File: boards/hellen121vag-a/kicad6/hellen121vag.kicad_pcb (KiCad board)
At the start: 2 copper layers, 164 x 118 mm, 9 parts, among them M1 Module-can-0.1, M2 Module-power5-0.1, M3 Module-mcu-0.1, M4 Module-input-0.1, M5 Module-knock-0.1, M6 Module-output-0.1, M7 Module-ign8-0.1, M8 Module-power12-0.1, P1 368255-2

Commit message: fresh kicad files
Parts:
- added C1: Cap, hellen-one-common:C0603, F.Cu at (115.7, 11.3)
- added D1: D_TVS_Array_4, hellen-one-common:SOT23-6, F.Cu at (121.5, 64.8)
- added F1: Fuse-Pad-Pad, hellen-one-common:PAD-1206-PAD, F.Cu at (188.1, 81.3)
- added F2: Fuse-Pad-Pad, hellen-one-common:PAD-1206-PAD, F.Cu at (183.9, 81.4)
- added J1: USB_B_Mini, hellen-one-common:USB-MINI-B-VERTICAL, F.Cu at (127.3, 9.27)
- added R1: Res_Array_4, hellen-one-common:R0603-4, F.Cu at (124.9, 64.7)
- added R2: Jumper-Pad-Pad, hellen-one-common:PAD-0805-PAD, F.Cu at (90.6, 82.1)
- added R3: Jumper-Pad-Pad, hellen-one-common:PAD-0805-PAD, F.Cu at (87.5, 82.4)
- added R4: Jumper-Pad-Pad, hellen-one-common:PAD-0805-PAD, F.Cu at (100.3, 82.2)
- added R5: Res_Array_4, hellen-one-common:R0603-4, F.Cu at (118.3, 64.7)
- added R6: Res, hellen-one-common:R0603, F.Cu at (102.6, 69.4)
- added R7: Res, hellen-one-common:R0603, F.Cu at (101.2, 69.4)
- added R8: Jumper-Pad-Pad, hellen-one-common:PAD-0805-PAD, F.Cu at (95.2, 82.3)
- added R9: Jumper-Pad-Pad, hellen-one-common:PAD-0805-PAD, F.Cu at (75.9, 82.6)
- added S1: Button_SPST, hellen-one-common:SMD-2_2.9x3.9x1.7, F.Cu at (112.1, 6.44)
- added S2: Button_SPST, hellen-one-common:SMD-2_2.9x3.9x1.7, F.Cu at (116.0, 6.42)
- added V10: Pad, hellen-one-common:PAD-TH, F.Cu at (122.6, 77.9)
- added V11: Pad, hellen-one-common:PAD-TH, F.Cu at (117.5, 77.9)
- added V12: Pad, hellen-one-common:PAD-TH, F.Cu at (113.0, 82.1)
- added V13: Pad, hellen-one-common:PAD-TH, F.Cu at (108.0, 82.1)
- added V14: Pad, hellen-one-common:PAD-TH, F.Cu at (104.9, 77.8)
- added V17: Pad, hellen-one-common:PAD-TH, F.Cu at (102.9, 82.1)
- added V20: Pad, hellen-one-common:PAD-TH, F.Cu at (95.5, 77.7)
- added V28: Pad, hellen-one-common:PAD-TH, F.Cu at (125.1, 77.9)
- added V40: Pad, hellen-one-common:PAD-TH, F.Cu at (93.0, 77.7)
- added V41: Pad, hellen-one-common:PAD-TH, F.Cu at (90.5, 77.7)
- added V43: Pad, hellen-one-common:PAD-TH, F.Cu at (85.5, 77.7)
- added V44: Pad, hellen-one-common:PAD-TH, F.Cu at (131.4, 77.9)
- added V45: Pad, hellen-one-common:PAD-TH, F.Cu at (129.3, 82.5)
- added V46: Pad, hellen-one-common:PAD-TH, F.Cu at (126.1, 82.5)
- added V48: Pad, hellen-one-common:PAD-TH, F.Cu at (120.0, 77.9)
- added V49: Pad, hellen-one-common:PAD-TH, F.Cu at (119.3, 82.4)
- added V51: Pad, hellen-one-common:PAD-TH, F.Cu at (110.5, 82.1)
- added V52: Pad, hellen-one-common:PAD-TH, F.Cu at (105.4, 82.1)
- added V56: Pad, hellen-one-common:PAD-TH, F.Cu at (101.7, 77.8)
- added V61: Pad, hellen-one-common:PAD-TH, F.Cu at (88.0, 77.7)
- added V63: Pad, hellen-one-common:PAD-TH, F.Cu at (133.4, 82.4)
- added V64: Pad, hellen-one-common:PAD-TH, F.Cu at (127.7, 77.9)
- added V66: Pad, hellen-one-common:PAD-TH, F.Cu at (139.2, 73.8)
- added V67: Pad, hellen-one-common:PAD-TH, F.Cu at (134.5, 77.8)
- added V68: Pad, hellen-one-common:PAD-TH, F.Cu at (137.7, 77.7)
- added V69: Pad, hellen-one-common:PAD-TH, F.Cu at (137.7, 82.1)
- added V70: Pad, hellen-one-common:PAD-TH, F.Cu at (140.8, 77.7)
- added V71: Pad, hellen-one-common:PAD-TH, F.Cu at (140.9, 82.1)
- added V74: Pad, hellen-one-common:PAD-TH, F.Cu at (80.4, 77.8)
- added V80: Pad, hellen-one-common:PAD-TH, F.Cu at (82.9, 77.7)
- added V9: Pad, hellen-one-common:PAD-TH, F.Cu at (122.9, 82.4)
- added VIN1: Pad, hellen-one-common:PAD-TH, F.Cu at (90.7, 68.8)
- added VIN2: Pad, hellen-one-common:PAD-TH, F.Cu at (99.2, 68.8)
- added VIN3: Pad, hellen-one-common:PAD-TH, F.Cu at (96.4, 68.8)
- added VIN4: Pad, hellen-one-common:PAD-TH, F.Cu at (93.5, 68.8)
- added VOUT1: Pad, hellen-one-common:PAD-TH, F.Cu at (152.9, 76.0)
- added VOUT2: Pad, hellen-one-common:PAD-TH, F.Cu at (162.4, 75.6)
- added VOUT3: Pad, hellen-one-common:PAD-TH, F.Cu at (166.0, 75.8)
- moved M5 23.3 mm to (64.3, 54.8)
- moved M8 12.0 mm to (120.8, 67.7)
- moved M6 10.8 mm to (140.8, 66.4)
- moved M7 9.92 mm to (72.4, 26.8)
- moved M4 9.40 mm to (85.0, 66.7)
- moved M3 8.56 mm to (84.9, 51.4)
- moved M1 1.99 mm to (85.2, 13.1)
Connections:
- M1 pad S1: unconnected-(M1-PadS1) -> /CANL
- M1 pad S2: unconnected-(M1-PadS2) -> /CANH
- M3 pad E10: unconnected-(M3-PadE10) -> /VVT1_1
- M3 pad E12: unconnected-(M3-PadE12) -> /WASTEGATE
- M3 pad E14: unconnected-(M3-PadE14) -> /COIL_A1
- M3 pad E15: unconnected-(M3-PadE15) -> /COIL_A2
- M3 pad E16: unconnected-(M3-PadE16) -> /VVT2_B1
- M3 pad E17: unconnected-(M3-PadE17) -> /VVT2_B2
- M3 pad E18: unconnected-(M3-PadE18) -> /IDLE
- M3 pad E19: unconnected-(M3-PadE19) -> /FUEL_CONSUM
- M3 pad E20: unconnected-(M3-PadE20) -> /VVT1_1
- M3 pad E21: unconnected-(M3-PadE21) -> /VVT1_2
- M3 pad E22: unconnected-(M3-PadE22) -> /CE
- M3 pad E25: unconnected-(M3-PadE25) -> /INJ1
- M3 pad E26: unconnected-(M3-PadE26) -> /INJ2
- M3 pad E27: unconnected-(M3-PadE27) -> /TACH
- M3 pad E28: unconnected-(M3-PadE28) -> /OUT3
- M3 pad E29: unconnected-(M3-PadE29) -> /INJ3
- M3 pad E30: unconnected-(M3-PadE30) -> /INJ4
- M3 pad E31: unconnected-(M3-PadE31) -> /INJ5
- M3 pad E32: unconnected-(M3-PadE32) -> /INJ6
- M3 pad E33: unconnected-(M3-PadE33) -> /INJ7
- M3 pad E34: unconnected-(M3-PadE34) -> /INJ8
- M3 pad E6: unconnected-(M3-PadE6) -> /MAIN
- M3 pad E7: unconnected-(M3-PadE7) -> /OUT1
- M3 pad E8: unconnected-(M3-PadE8) -> /PUMP
- M3 pad E9: unconnected-(M3-PadE9) -> /OUT2
- M3 pad N14: unconnected-(M3-PadN14) -> +3V3
- M3 pad N22: unconnected-(M3-PadN22) -> /NRESET
- M3 pad N26: unconnected-(M3-PadN26) -> /BOOT0
- M3 pad N27: unconnected-(M3-PadN27) -> /VBUS
- M3 pad N28: unconnected-(M3-PadN28) -> /USBP
- M3 pad N29: unconnected-(M3-PadN29) -> /USBM
- M3 pad S12: unconnected-(M3-PadS12) -> /KNOCK1
- M3 pad S13: unconnected-(M3-PadS13) -> /CRANK
- M3 pad S14: unconnected-(M3-PadS14) -> /VSS
- M3 pad S15: unconnected-(M3-PadS15) -> /CAM1
- M3 pad S16: unconnected-(M3-PadS16) -> /O2S
- M3 pad S17: unconnected-(M3-PadS17) -> /TPS1
- M3 pad S18: unconnected-(M3-PadS18) -> /CLT
- M3 pad S19: unconnected-(M3-PadS19) -> /IAT
- M3 pad S20: unconnected-(M3-PadS20) -> /MAF
- M3 pad S21: unconnected-(M3-PadS21) -> /MAP2
- M3 pad S22: unconnected-(M3-PadS22) -> /A2
- M3 pad S23: unconnected-(M3-PadS23) -> /A4
- M3 pad S24: unconnected-(M3-PadS24) -> /TPS2
- M3 pad S25: unconnected-(M3-PadS25) -> /PPS2
- M3 pad S26: unconnected-(M3-PadS26) -> /A3
- M3 pad S27: unconnected-(M3-PadS27) -> /CAM2
- M3 pad S28: unconnected-(M3-PadS28) -> /RES1
- M3 pad S29: unconnected-(M3-PadS29) -> /PPS1
- M3 pad S3: unconnected-(M3-PadS3) -> /D1
- M3 pad S30: unconnected-(M3-PadS30) -> /A1
- M3 pad S31: unconnected-(M3-PadS31) -> /RES2
- M3 pad S33: +5V -> V5A
- M3 pad S4: unconnected-(M3-PadS4) -> /D2
- M3 pad S5: unconnected-(M3-PadS5) -> /D3
- M3 pad S6: unconnected-(M3-PadS6) -> /D4
- M4 pad E6: +5V -> V5A
- M4 pad J1: +5V -> V5A
- M4 pad J10: unconnected-(M4-PadJ10) -> V5A
- M4 pad J11: unconnected-(M4-PadJ11) -> GNDA
- M4 pad J12: unconnected-(M4-PadJ12) -> GNDA
- M4 pad J13: unconnected-(M4-PadJ13) -> GNDA
- M4 pad J14: unconnected-(M4-PadJ14) -> GNDA
- M4 pad J17: unconnected-(M4-PadJ17) -> V5A
- M4 pad J18: unconnected-(M4-PadJ18) -> V5A
- M4 pad J19: unconnected-(M4-PadJ19) -> V5A
- M4 pad J20: unconnected-(M4-PadJ20) -> V5A
- M4 pad J21: unconnected-(M4-PadJ21) -> V5A
- M4 pad J22: unconnected-(M4-PadJ22) -> GNDA
- M4 pad J24: unconnected-(M4-PadJ24) -> GNDA
- M4 pad J3: unconnected-(M4-PadJ3) -> GNDA
- M4 pad J4: unconnected-(M4-PadJ4) -> GNDA
- M4 pad J5: unconnected-(M4-PadJ5) -> V5A
- M4 pad J6: unconnected-(M4-PadJ6) -> GNDA
- M4 pad J7: unconnected-(M4-PadJ7) -> V5A
- M4 pad J8: unconnected-(M4-PadJ8) -> GNDA
- M4 pad J9: unconnected-(M4-PadJ9) -> V5A
- M4 pad N1: unconnected-(M4-PadN1) -> V5A
- M4 pad N10: unconnected-(M4-PadN10) -> /TPS2
- M4 pad N11: unconnected-(M4-PadN11) -> /A4
- M4 pad N12: unconnected-(M4-PadN12) -> /A2
- M4 pad N13: unconnected-(M4-PadN13) -> /MAP2
- M4 pad N14: unconnected-(M4-PadN14) -> /MAF
- M4 pad N15: unconnected-(M4-PadN15) -> /IAT
- M4 pad N16: unconnected-(M4-PadN16) -> /CLT
- M4 pad N17: unconnected-(M4-PadN17) -> /TPS1
- M4 pad N18: unconnected-(M4-PadN18) -> /AFR
- M4 pad N19: unconnected-(M4-PadN19) -> /CAM1
- M4 pad N2: unconnected-(M4-PadN2) -> GNDA
- M4 pad N20: unconnected-(M4-PadN20) -> /VSS
- M4 pad N21: unconnected-(M4-PadN21) -> /CRANK
- M4 pad N22: unconnected-(M4-PadN22) -> /KNOCK1
- M4 pad N24: unconnected-(M4-PadN24) -> /KNOCK2
- M4 pad N3: unconnected-(M4-PadN3) -> /RES2
- M4 pad N4: unconnected-(M4-PadN4) -> /A1
- M4 pad N5: unconnected-(M4-PadN5) -> /PPS1
- M4 pad N6: unconnected-(M4-PadN6) -> /MAF
- M4 pad N7: unconnected-(M4-PadN7) -> /CAM2
- M4 pad N8: unconnected-(M4-PadN8) -> /A3
- M4 pad N9: unconnected-(M4-PadN9) -> /PPS2
- M4 pad S10: unconnected-(M4-PadS10) -> /IN_TPS1
- M4 pad S11: unconnected-(M4-PadS11) -> /IN_MAF
- M4 pad S12: unconnected-(M4-PadS12) -> /IN_MAP2
- M4 pad S13: unconnected-(M4-PadS13) -> /VREF2
- M4 pad S14: unconnected-(M4-PadS14) -> /VREF1
- M4 pad S15: unconnected-(M4-PadS15) -> /IN_CLT
- M4 pad S16: unconnected-(M4-PadS16) -> /IN_IAT
- M4 pad S17: unconnected-(M4-PadS17) -> /IN_TPS2
- M4 pad S18: unconnected-(M4-PadS18) -> /IN_PPS2
- M4 pad S19: unconnected-(M4-PadS19) -> /IN_A2
- M4 pad S20: unconnected-(M4-PadS20) -> /IN_A3
- M4 pad S21: unconnected-(M4-PadS21) -> /IN_CAM2
- M4 pad S22: unconnected-(M4-PadS22) -> /IN_A4
- M4 pad S23: unconnected-(M4-PadS23) -> /IN_RES1
- M4 pad S24: unconnected-(M4-PadS24) -> /IN_PPS1
- M4 pad S25: unconnected-(M4-PadS25) -> /IN_A1
- M4 pad S26: unconnected-(M4-PadS26) -> /IN_RES2
- M4 pad S3: unconnected-(M4-PadS3) -> /IN_KNOCK2
- M4 pad S5: unconnected-(M4-PadS5) -> /IN_CAM1
- M4 pad S6: unconnected-(M4-PadS6) -> /IN_VSS
- M4 pad S7: unconnected-(M4-PadS7) -> /IN_KNOCK1
- M4 pad S8: unconnected-(M4-PadS8) -> /IN_CRANK
- M4 pad S9: unconnected-(M4-PadS9) -> /IN_AFR
- M5 pad E1: +5V -> V5A
- M5 pad E3: unconnected-(M5-PadE3) -> /IN_KNOCK1
- M5 pad W1: unconnected-(M5-PadW1) -> /IN_KNOCK1_RAW
- M5 pad W2: unconnected-(M5-PadW2) -> /VREF2
- M6 pad S1: unconnected-(M6-PadS1) -> /OUT_COIL_A1
- M6 pad S10: unconnected-(M6-PadS10) -> /OUT_PUMP
- M6 pad S11: +5V -> V12_RAW
- M6 pad S12: unconnected-(M6-PadS12) -> Net-(M6-PadS12)
- M6 pad S13: unconnected-(M6-PadS13) -> /OUT_VVT1_1
- M6 pad S14: unconnected-(M6-PadS14) -> /OUT_VVT1_1
- M6 pad S15: unconnected-(M6-PadS15) -> /OUT_INJ6
- M6 pad S16: unconnected-(M6-PadS16) -> /OUT_INJ2
- M6 pad S17: unconnected-(M6-PadS17) -> /OUT_INJ3
- M6 pad S18: unconnected-(M6-PadS18) -> /OUT_INJ1
- M6 pad S2: unconnected-(M6-PadS2) -> /OUT_COIL_A2
- M6 pad S4: unconnected-(M6-PadS4) -> /OUT_VVT2_B1
- M6 pad S5: unconnected-(M6-PadS5) -> /OUT_VVT2_B2
- M6 pad S6: unconnected-(M6-PadS6) -> /OUT_FUEL_CONSUM
- M6 pad S7: unconnected-(M6-PadS7) -> /OUT_IDLE
- M6 pad S8: unconnected-(M6-PadS8) -> Net-(M6-PadS8)
- M6 pad W1: unconnected-(M6-PadW1) -> /OUT_VVT1_2
- M6 pad W10: unconnected-(M6-PadW10) -> /OUT_INJ5
- M6 pad W11: unconnected-(M6-PadW11) -> /OUT_INJ8
- M6 pad W12: unconnected-(M6-PadW12) -> /OUT_INJ7
- M6 pad W13: unconnected-(M6-PadW13) -> /OUT_MAIN
- M6 pad W15: unconnected-(M6-PadW15) -> /INJ8
- M6 pad W16: unconnected-(M6-PadW16) -> /INJ7
- M6 pad W17: unconnected-(M6-PadW17) -> /INJ6
- M6 pad W18: unconnected-(M6-PadW18) -> /INJ5
- M6 pad W19: unconnected-(M6-PadW19) -> /INJ4
- M6 pad W2: unconnected-(M6-PadW2) -> /OUT_VVT1_2
- M6 pad W20: unconnected-(M6-PadW20) -> /INJ3
- M6 pad W21: unconnected-(M6-PadW21) -> /OUT3
- M6 pad W22: unconnected-(M6-PadW22) -> /FUEL_CONSUM
- M6 pad W23: unconnected-(M6-PadW23) -> /INJ2
- M6 pad W24: unconnected-(M6-PadW24) -> /INJ1
- M6 pad W25: unconnected-(M6-PadW25) -> /CE
- M6 pad W26: unconnected-(M6-PadW26) -> /VVT1_2
- M6 pad W27: unconnected-(M6-PadW27) -> /VVT1_1
- M6 pad W28: unconnected-(M6-PadW28) -> /TACH
- M6 pad W29: unconnected-(M6-PadW29) -> /VVT1_2
- M6 pad W3: unconnected-(M6-PadW3) -> /OUT_CE
- M6 pad W30: unconnected-(M6-PadW30) -> /VVT2_B2
- M6 pad W31: unconnected-(M6-PadW31) -> /VVT2_B1
- M6 pad W32: unconnected-(M6-PadW32) -> /COIL_A2
- M6 pad W33: unconnected-(M6-PadW33) -> /COIL_A1
- M6 pad W34: unconnected-(M6-PadW34) -> /WASTEGATE
- M6 pad W35: unconnected-(M6-PadW35) -> /PUMP
- M6 pad W36: unconnected-(M6-PadW36) -> /VVT1_1
- M6 pad W37: unconnected-(M6-PadW37) -> /OUT2
- M6 pad W38: unconnected-(M6-PadW38) -> /IDLE
- M6 pad W39: unconnected-(M6-PadW39) -> /OUT1
- M6 pad W4: unconnected-(M6-PadW4) -> /OUT_WASTEGATE
- M6 pad W40: unconnected-(M6-PadW40) -> /MAIN
- M6 pad W6: unconnected-(M6-PadW6) -> /OUT_TACH
- M6 pad W7: unconnected-(M6-PadW7) -> /OUT_INJ4
- M6 pad W9: unconnected-(M6-PadW9) -> Net-(M6-PadW9)
- M7 pad S1: unconnected-(M7-PadS1) -> /OUT_IGN8
- M7 pad S2: unconnected-(M7-PadS2) -> /OUT_IGN7
- M7 pad S3: unconnected-(M7-PadS3) -> /OUT_IGN6
- M7 pad S4: unconnected-(M7-PadS4) -> /OUT_IGN5
- M7 pad S5: unconnected-(M7-PadS5) -> /OUT_IGN4
- M7 pad S6: unconnected-(M7-PadS6) -> /OUT_IGN3
- M7 pad S7: unconnected-(M7-PadS7) -> /OUT_IGN2
- M7 pad S8: unconnected-(M7-PadS8) -> /OUT_IGN1
- M7 pad V1: /IGN1 -> /IGN8
- M7 pad V2: /IGN8 -> /IGN7
- M8 pad E2: +5V -> V12_RAW
- M8 pad V1: +12V -> Net-(M8-PadV1)
- M8 pad V3: unconnected-(M8-PadV3) -> /IN_VIGN
- M8 pad V4: unconnected-(M8-PadV4) -> /V12_PERM
- P1 pad 1: unconnected-(P1-Pad1) -> GND
- P1 pad 10: unconnected-(P1-Pad10) -> Net-(P1-Pad10)
- P1 pad 101: unconnected-(P1-Pad101) -> /IN_MAP2
- P1 pad 102: unconnected-(P1-Pad102) -> /OUT_IGN1
- P1 pad 103: unconnected-(P1-Pad103) -> /OUT_IGN5
- P1 pad 104: unconnected-(P1-Pad104) -> /OUT_WASTEGATE
- P1 pad 105: unconnected-(P1-Pad105) -> /OUT_IDLE
- P1 pad 106: unconnected-(P1-Pad106) -> /IN_KNOCK1_RAW
- P1 pad 107: unconnected-(P1-Pad107) -> /IN_KNOCK2_RAW
- P1 pad 108: unconnected-(P1-Pad108) -> GNDA
- P1 pad 11: unconnected-(P1-Pad11) -> Net-(P1-Pad11)
- P1 pad 110: unconnected-(P1-Pad110) -> /OUT_IGN6
- P1 pad 111: unconnected-(P1-Pad111) -> /OUT_IGN3
- P1 pad 112: unconnected-(P1-Pad112) -> /OUT_INJ6
- P1 pad 113: unconnected-(P1-Pad113) -> /OUT_INJ5
- P1 pad 115: unconnected-(P1-Pad115) -> /OUT_VVT1_2
- P1 pad 117: unconnected-(P1-Pad117) -> /OUT_COIL_A1
- P1 pad 118: unconnected-(P1-Pad118) -> /OUT_COIL_A2
- P1 pad 12: unconnected-(P1-Pad12) -> Net-(P1-Pad12)
- P1 pad 120: unconnected-(P1-Pad120) -> /OUT_VVT2_B2
- P1 pad 121: unconnected-(P1-Pad121) -> Net-(F2-Pad1)
- P1 pad 13: unconnected-(P1-Pad13) -> Net-(P1-Pad13)
- P1 pad 14: unconnected-(P1-Pad14) -> /IN_AFR
- P1 pad 17: unconnected-(P1-Pad17) -> Net-(P1-Pad17)
- P1 pad 18: unconnected-(P1-Pad18) -> /OUT_VVT2_B1
- P1 pad 19: unconnected-(P1-Pad19) -> /OUT_INJ7
- P1 pad 2: unconnected-(P1-Pad2) -> GND
- P1 pad 20: unconnected-(P1-Pad20) -> Net-(P1-Pad20)
- P1 pad 21: unconnected-(P1-Pad21) -> Net-(P1-Pad21)
- P1 pad 22: unconnected-(P1-Pad22) -> /OUT_VVT1_1
- P1 pad 23: unconnected-(P1-Pad23) -> Net-(P1-Pad23)
- P1 pad 24: unconnected-(P1-Pad24) -> /OUT_INJ8
- P1 pad 26: unconnected-(P1-Pad26) -> /IN_IAT
- P1 pad 27: unconnected-(P1-Pad27) -> GNDA
- P1 pad 28: unconnected-(P1-Pad28) -> Net-(P1-Pad28)
- P1 pad 29: unconnected-(P1-Pad29) -> /IN_MAF
- P1 pad 3: unconnected-(P1-Pad3) -> Net-(F1-Pad1)
- P1 pad 32: unconnected-(P1-Pad32) -> GND
- P1 pad 33: unconnected-(P1-Pad33) -> GNDA
- P1 pad 34: unconnected-(P1-Pad34) -> /IN_PPS1
- P1 pad 35: unconnected-(P1-Pad35) -> /IN_PPS2
- P1 pad 36: unconnected-(P1-Pad36) -> GNDA
- P1 pad 37: unconnected-(P1-Pad37) -> Net-(P1-Pad37)
- P1 pad 38: unconnected-(P1-Pad38) -> /IN_RES1
- P1 pad 39: unconnected-(P1-Pad39) -> /IN_RES2
- P1 pad 40: unconnected-(P1-Pad40) -> Net-(P1-Pad40)
- P1 pad 41: unconnected-(P1-Pad41) -> Net-(P1-Pad41)
- P1 pad 43: unconnected-(P1-Pad43) -> Net-(P1-Pad43)
- P1 pad 44: unconnected-(P1-Pad44) -> Net-(P1-Pad44)
- P1 pad 45: unconnected-(P1-Pad45) -> Net-(P1-Pad45)
- P1 pad 46: unconnected-(P1-Pad46) -> Net-(P1-Pad46)
- P1 pad 47: unconnected-(P1-Pad47) -> /OUT_CE
- P1 pad 48: unconnected-(P1-Pad48) -> Net-(P1-Pad48)
- P1 pad 49: unconnected-(P1-Pad49) -> Net-(P1-Pad49)
- P1 pad 50: unconnected-(P1-Pad50) -> GNDA
- P1 pad 51: unconnected-(P1-Pad51) -> Net-(P1-Pad51)
- P1 pad 52: unconnected-(P1-Pad52) -> Net-(P1-Pad52)
- P1 pad 53: unconnected-(P1-Pad53) -> V5A
- P1 pad 54: unconnected-(P1-Pad54) -> /IN_VSS
- P1 pad 55: unconnected-(P1-Pad55) -> /IN_D1
- P1 pad 56: unconnected-(P1-Pad56) -> Net-(P1-Pad56)
- P1 pad 57: unconnected-(P1-Pad57) -> /IN_D2
- P1 pad 58: unconnected-(P1-Pad58) -> /CANL
- P1 pad 59: unconnected-(P1-Pad59) -> GND
- P1 pad 60: unconnected-(P1-Pad60) -> /CANH
- P1 pad 61: unconnected-(P1-Pad61) -> Net-(P1-Pad61)
- P1 pad 62: unconnected-(P1-Pad62) -> /V12_PERM
- P1 pad 63: unconnected-(P1-Pad63) -> Net-(P1-Pad63)
- P1 pad 64: unconnected-(P1-Pad64) -> Net-(P1-Pad64)
- P1 pad 65: unconnected-(P1-Pad65) -> /OUT_PUMP
- P1 pad 66: unconnected-(P1-Pad66) -> Net-(P1-Pad66)
- P1 pad 67: unconnected-(P1-Pad67) -> Net-(P1-Pad67)
- P1 pad 68: unconnected-(P1-Pad68) -> Net-(P1-Pad68)
- P1 pad 69: unconnected-(P1-Pad69) -> Net-(P1-Pad69)
- P1 pad 7: unconnected-(P1-Pad7) -> /OUT_IGN2
- P1 pad 70: unconnected-(P1-Pad70) -> Net-(P1-Pad70)
- P1 pad 71: unconnected-(P1-Pad71) -> Net-(P1-Pad71)
- P1 pad 72: unconnected-(P1-Pad72) -> V5A
- P1 pad 73: unconnected-(P1-Pad73) -> V5A
- P1 pad 74: unconnected-(P1-Pad74) -> Net-(P1-Pad74)
- P1 pad 75: unconnected-(P1-Pad75) -> /IN_D3
- P1 pad 76: unconnected-(P1-Pad76) -> /IN_D4
- P1 pad 8: unconnected-(P1-Pad8) -> /OUT_IGN7
- P1 pad 80: unconnected-(P1-Pad80) -> Net-(P1-Pad80)
- P1 pad 81: unconnected-(P1-Pad81) -> /OUT_FUEL_CONSUM
- P1 pad 82: unconnected-(P1-Pad82) -> /IN_CRANK
- P1 pad 83: unconnected-(P1-Pad83) -> V5A
- P1 pad 84: unconnected-(P1-Pad84) -> /IN_TPS2
- P1 pad 85: unconnected-(P1-Pad85) -> /IN_IAT
- P1 pad 86: unconnected-(P1-Pad86) -> /IN_CAM1
- P1 pad 87: unconnected-(P1-Pad87) -> /IN_CAM2
- P1 pad 88: unconnected-(P1-Pad88) -> /OUT_INJ4
- P1 pad 89: unconnected-(P1-Pad89) -> /OUT_INJ2
- P1 pad 9: unconnected-(P1-Pad9) -> Net-(P1-Pad9)
- P1 pad 90: unconnected-(P1-Pad90) -> /VREF1
- P1 pad 91: unconnected-(P1-Pad91) -> GNDA
- P1 pad 92: unconnected-(P1-Pad92) -> /IN_TPS
- P1 pad 93: unconnected-(P1-Pad93) -> /IN_CLT
- P1 pad 94: unconnected-(P1-Pad94) -> /OUT_IGN4
- P1 pad 95: unconnected-(P1-Pad95) -> /OUT_IGN8
- P1 pad 96: unconnected-(P1-Pad96) -> /OUT_INJ1
- P1 pad 97: unconnected-(P1-Pad97) -> /OUT_INJ3
- P1 pad 98: unconnected-(P1-Pad98) -> V5A
- P1 pad 99: unconnected-(P1-Pad99) -> GNDA
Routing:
- net Net-(F1-Pad1): track 0.00 -> 139.9 mm
- net unconnected-(P1-Pad115): track 66.9 -> 0.00 mm
- net unconnected-(P1-Pad72): track 66.9 -> 0.00 mm
- net unconnected-(P1-Pad73): track 64.3 -> 0.00 mm
- net unconnected-(P1-Pad74): track 60.2 -> 0.00 mm
- net unconnected-(P1-Pad75): track 57.5 -> 0.00 mm
- net /IN_IAT: track 0.00 -> 52.0 mm
- net Net-(P1-Pad74): track 0.00 -> 51.2 mm
- net Net-(P1-Pad71): track 0.00 -> 50.0 mm
- net unconnected-(P1-Pad71): track 49.9 -> 0.00 mm
- net unconnected-(P1-Pad89): track 49.6 -> 0.00 mm
- net /OUT_INJ2: track 0.00 -> 49.6 mm
- net unconnected-(P1-Pad70): track 49.5 -> 0.00 mm
- net Net-(P1-Pad68): track 0.00 -> 46.5 mm
- net /OUT_IGN2: track 0.00 -> 45.5 mm
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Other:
- outline, holes or cut-outs redrawn

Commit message: update kicad files
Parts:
- moved R9 21.4 mm to (97.3, 82.3)
- moved F1 18.3 mm to (169.8, 81.2)
- moved VOUT1 17.7 mm to (136.2, 70.1)
- moved VOUT3 15.6 mm to (151.4, 70.0)
- moved VOUT2 14.9 mm to (148.6, 70.0)
- moved V66 11.9 mm to (128.1, 78.0)
- moved V74 11.3 mm to (91.6, 77.7)
- moved F2 11.2 mm to (172.7, 81.2)
- moved V70 7.36 mm to (133.4, 78.0)
- moved V68 6.91 mm to (130.8, 78.0)
- moved V14 6.52 mm to (109.5, 82.3)
- moved V44 6.05 mm to (125.4, 78.0)
- moved V52 5.71 mm to (109.4, 78.0)
- moved M2 5.28 mm to (133.2, 18.7)
- moved V9 5.23 mm to (120.1, 78.0)
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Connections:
- M3 pad E20: /VVT1_1 -> unconnected-(M3-PadE20)
- M3 pad S16: /O2S -> /AFR
- M3 pad W10: +3V3 -> /IGN_V33
- M3 pad W4: /IGN6 -> /IGN4
- M3 pad W5: /IGN7 -> /IGN5
- M3 pad W6: /IGN1 -> /IGN6
- M3 pad W7: /IGN1 -> /IGN7
- M3 pad W9: +5V -> /IGN_V5
- M4 pad N6: /MAF -> /RES1
- M7 pad V10: +3V3 -> /IGN_V33
- M7 pad V9: +5V -> /IGN_V5
- M8 pad V1: Net-(M8-PadV1) -> +12V
- P1 pad 92: /IN_TPS -> /IN_TPS1
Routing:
- net /OUT_IGN6: track 7.78 -> 290.4 mm, vias 0 -> 1
- net /OUT_IGN8: track 16.6 -> 291.6 mm, vias 0 -> 1
- net /OUT_IGN4: track 16.6 -> 290.2 mm, vias 0 -> 1
- net /OUT_IGN5: track 11.2 -> 282.0 mm, vias 0 -> 1
- net /OUT_IGN1: track 11.2 -> 281.8 mm, vias 0 -> 1
- net /OUT_IGN3: track 7.78 -> 277.9 mm, vias 0 -> 1
- net +5V: track 0.00 -> 171.2 mm, vias 0 -> 5
- net /IN_KNOCK1_RAW: track 7.78 -> 129.1 mm, vias 0 -> 1
- net GNDA: track 15.6 -> 134.2 mm, vias 0 -> 2
- net /CANH: track 16.8 -> 118.3 mm, vias 0 -> 1
- net /CANL: track 16.8 -> 118.2 mm, vias 0 -> 1
- net V5A: track 16.7 -> 113.2 mm, vias 0 -> 3
- net /IN_D3: track 0.00 -> 92.2 mm, vias 0 -> 1
- net /OUT_VVT2_B1: track 7.88 -> 92.3 mm, vias 0 -> 3
- net /OUT_FUEL_CONSUM: track 19.6 -> 102.2 mm, vias 0 -> 1
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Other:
- outline, holes or cut-outs redrawn
- board text added: "Hellen121vag"
- board text added: "PROG"
- board text added: "RESET"
- board text added: "http://rusefi.com/s/hellen121vag"
- board text added: "© andreika, 2021"

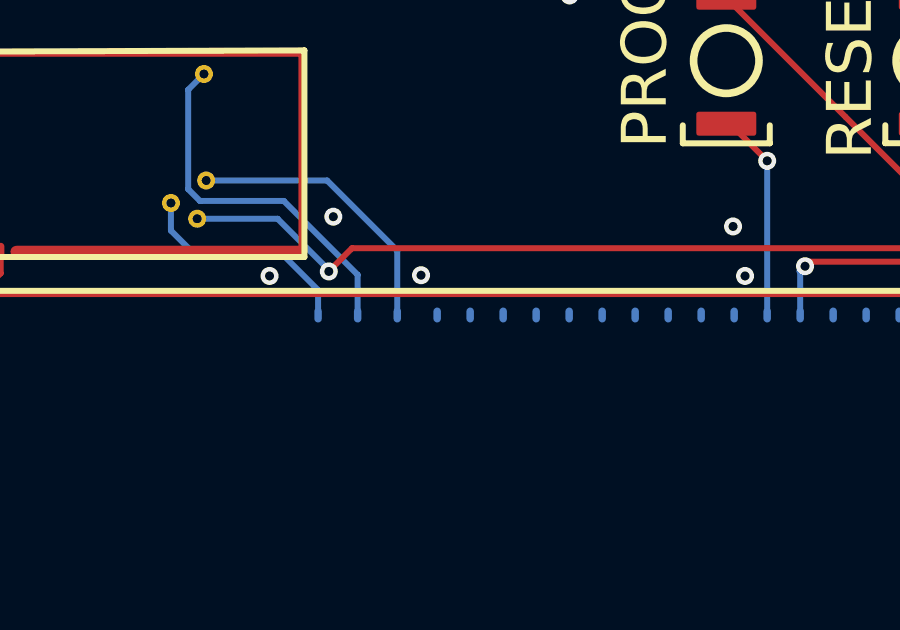
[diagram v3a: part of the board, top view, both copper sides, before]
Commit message: update kicad files after mod.refactoring
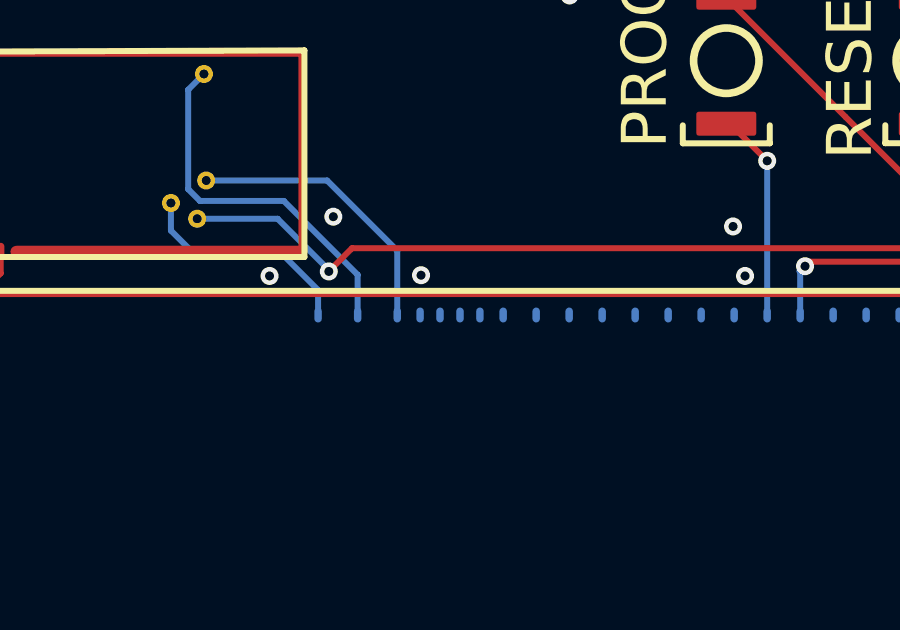
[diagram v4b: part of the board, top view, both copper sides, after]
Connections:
- M3 pad N14: +3V3 -> unconnected-(M3-PadN14)
- M3 pad N15: /VBAT -> unconnected-(M3-PadN15)
- M3 pad N16: unconnected-(M3-PadN16) -> +3V3
- M3 pad N17: unconnected-(M3-PadN17) -> /VBAT
- M3 pad N22: /NRESET -> unconnected-(M3-PadN22)
- M3 pad N24: unconnected-(M3-PadN24) -> /NRESET
- M3 pad N26: /BOOT0 -> unconnected-(M3-PadN26)
- M3 pad N27: /VBUS -> unconnected-(M3-PadN27)
- M3 pad N28: /USBP -> /BOOT0
- M3 pad N29: /USBM -> /VBUS
- M3 pad N30: unconnected-(M3-PadN30) -> /USBP
- M4 pad E5: GND -> V5A

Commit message: wbo added
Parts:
- removed V51, V52, V70, V71: Pad, hellen-one-common:PAD-TH
- added M10: Module-can-0.1, hellen-one-can-0.1:can, F.Cu at (77.4, 36.9)
- added M9: Module-wbo-0.1, hellen-one-wbo-0.1:wbo, F.Cu at (62.7, 44.2)
- added R10: Jumper-Pad-Pad, hellen-one-common:PAD-0805-PAD, F.Cu at (59.0, 80.4)
- added R11: Jumper-Pad-Pad, hellen-one-common:PAD-0805-PAD, F.Cu at (56.7, 80.4)
- added R12: Jumper-Pad-Pad, hellen-one-common:PAD-0805-PAD, F.Cu at (61.3, 80.4)
- added R13: Jumper-Pad-Pad, hellen-one-common:PAD-0805-PAD, F.Cu at (54.4, 80.5)
- moved M5 22.8 mm to (83.8, 66.6), turned to 90 degrees
- moved M2 0.61 mm to (133.8, 18.7)
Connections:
- net /CANH renamed /CAN+
- net /CANL renamed /CAN-
- P1 pad 5: unconnected-(P1-Pad5) -> /LSU_HEAT-
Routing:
- net Net-(P1-Pad51): track 23.8 -> 83.1 mm, vias 0 -> 1
- net Net-(P1-Pad52): track 23.8 -> 80.4 mm, vias 0 -> 1
- net +5V: track 171.2 -> 225.0 mm, vias 5 -> 6
- net Net-(P1-Pad71): track 51.5 -> 80.5 mm, vias 0 -> 1
- net /VREF2: track 53.0 -> 26.7 mm
- net Net-(P1-Pad70): track 57.3 -> 77.4 mm, vias 0 -> 1
- net /IN_KNOCK1_RAW: track 129.1 -> 110.1 mm, vias 1 -> 3
- net /LSU_HEAT-: track 0.00 -> 15.3 mm
- net /LSU_CALIBR_RES: track 0.00 -> 15.1 mm
- net /LSU_PUMP_I: track 0.00 -> 11.5 mm
- net /LSU_SENSOR_U/PUMP_I: track 0.00 -> 8.01 mm
- net /IN_KNOCK1: track 40.6 -> 48.0 mm
- net Net-(M10-PadV2): track 0.00 -> 6.96 mm
- net GNDA: track 134.2 -> 127.3 mm
- net GND: track 14.3 -> 8.52 mm, vias 147 -> 297
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
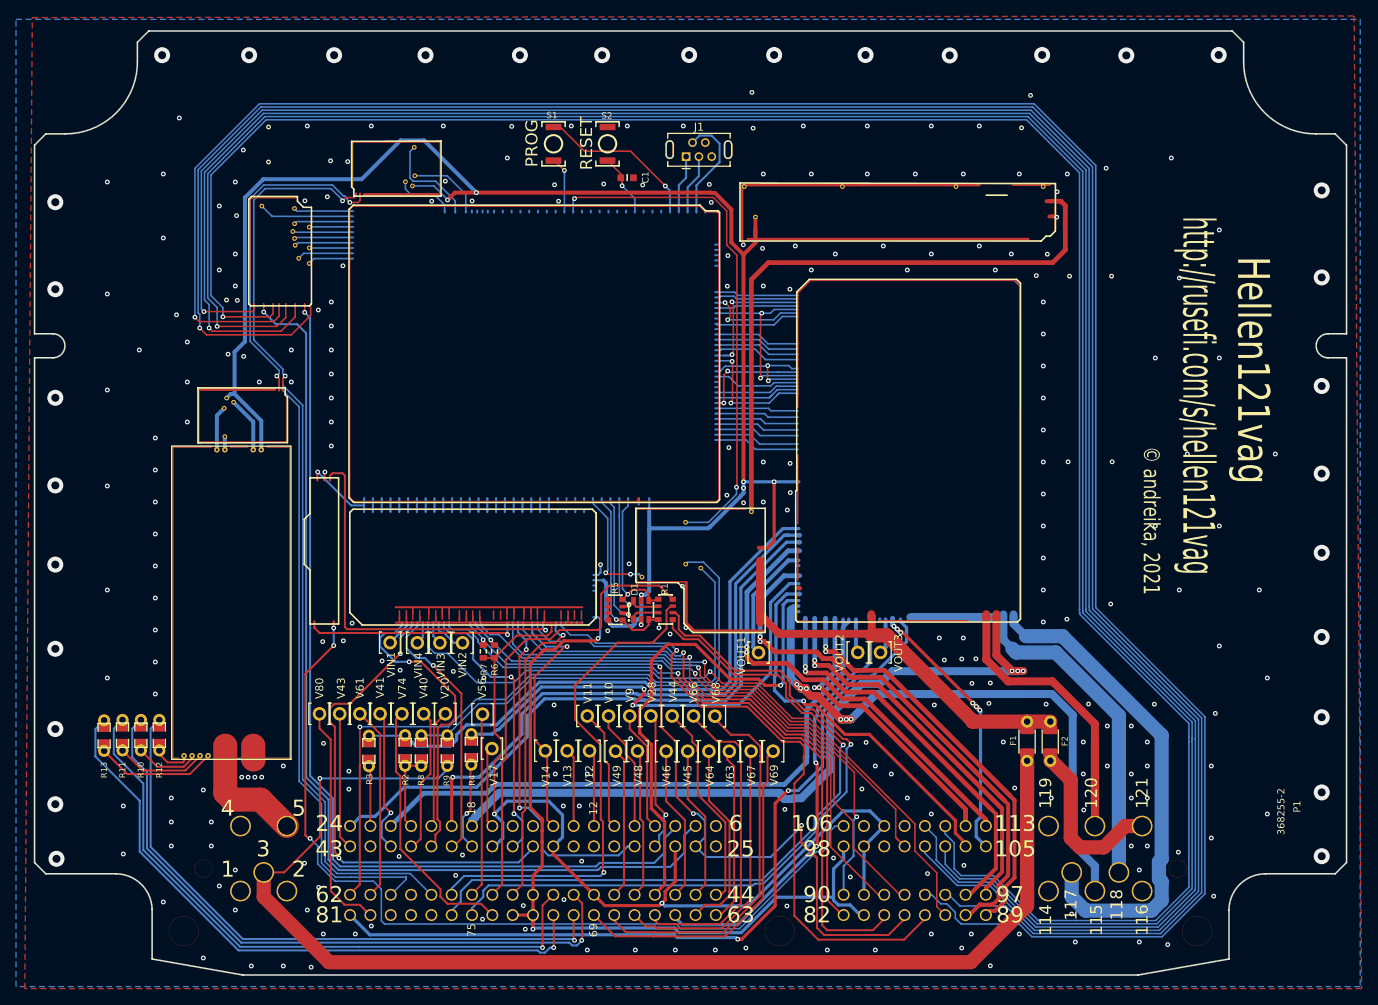
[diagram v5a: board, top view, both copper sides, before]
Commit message: Use vr module
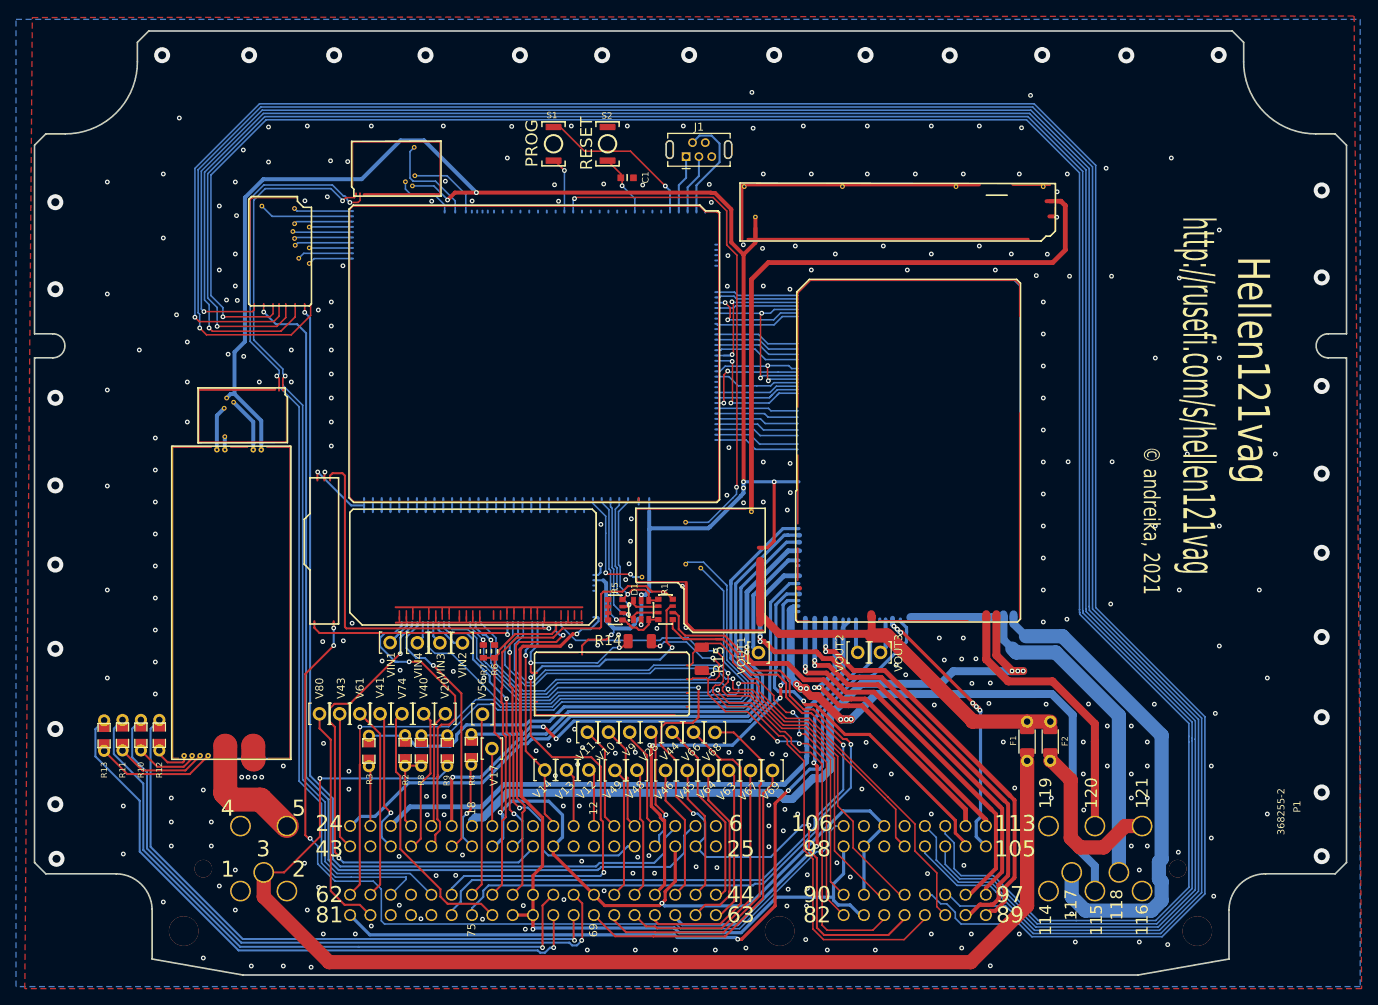
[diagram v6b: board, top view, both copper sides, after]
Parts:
- added M11: Module-vr-0.1, hellen-one-vr-0.1:vr, F.Cu at (107.9, 78.0)
- added R14: DNP, hellen-one-common:R1206, F.Cu at (121.4, 68.7)
- added R15: DNP, hellen-one-common:R1206, F.Cu at (129.1, 70.8)
- moved V12 2.40 mm to (115.0, 84.8)
- moved V13 2.40 mm to (112.2, 84.8)
- moved V14 2.40 mm to (109.5, 84.8)
- moved V48 2.40 mm to (121.0, 84.8)
- moved V63 2.40 mm to (132.5, 84.8)
- moved V67 2.40 mm to (135.2, 84.8)
- moved V69 2.40 mm to (137.9, 84.8)
- moved V45 2.40 mm to (127.3, 84.8)
- moved V46 2.40 mm to (124.6, 84.8)
- moved V49 2.40 mm to (118.2, 84.8)
- moved V64 2.40 mm to (129.9, 84.8)
- moved V10 2.03 mm to (117.5, 80.0)
- moved V11 2.03 mm to (114.8, 80.0)
- moved V28 2.03 mm to (122.8, 80.0)
- moved V44 2.03 mm to (125.4, 80.0)
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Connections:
- P1 pad 82: /IN_CRANK -> /IN_CRANK+
- P1 pad 90: /VREF1 -> /IN_CRANK-
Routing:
- net /IN_CRANK+: track 0.00 -> 56.0 mm, vias 0 -> 4
- net /IN_CRANK: track 66.4 -> 20.5 mm, vias 1 -> 2
- net /IN_CRANK-: track 0.00 -> 45.2 mm, vias 0 -> 2
- net /VREF1: track 72.2 -> 36.9 mm, vias 2 -> 1
- net /IN_D2: track 63.3 -> 76.9 mm, vias 1 -> 3
- net /OUT_CE: track 63.1 -> 52.7 mm, vias 1 -> 3
- net /IN_IAT: track 97.0 -> 104.4 mm
- net /IN_TPS1: track 68.2 -> 75.1 mm
- net /V12_PERM: track 83.7 -> 90.3 mm
- net /IN_VIGN: track 59.2 -> 65.7 mm
- net +5V: track 225.0 -> 231.5 mm, vias 6 -> 7
- net /OUT_MAIN: track 74.0 -> 78.5 mm
- net /IN_AFR: track 31.6 -> 27.2 mm
- net /IN_MAP2: track 65.2 -> 69.6 mm
- net Net-(P1-Pad12): track 10.3 -> 7.26 mm
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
